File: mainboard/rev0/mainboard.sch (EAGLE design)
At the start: 11 parts

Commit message: cleaned up schematic
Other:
- note added: "Bluetooth"
- note added: "PWR Management"
- moved on the sheet: C1, C2, R1, R2, R3, R4, R5
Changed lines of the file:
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@@
 <sheet>
 <plain>
-<text x="-33.02" y="60.96" size="5.08" layer="97">MCU (MSP430F5528)</text>
+<text x="-121.92" y="58.42" size="5.08" layer="97">MCU (MSP430F5528)</text>
+<wire x1="-370.84" y1="48.26" x2="-370.84" y2="-63.5" width="0.1524" layer="97"/>
+<wire x1="-370.84" y1="-63.5" x2="-152.4" y2="-63.5" width="0.1524" layer="97"/>
+<wire x1="-152.4" y1="-63.5" x2="-152.4" y2="48.26" width="0.1524" layer="97"/>
+<wire x1="-152.4" y1="48.26" x2="-370.84" y2="48.26" width="0.1524" layer="97"/>
+<wire x1="-124.46" y1="55.88" x2="119.38" y2="55.88" width="0.1524" layer="97"/>
+<wire x1="119.38" y1="55.88" x2="119.38" y2="-68.58" width="0.1524" layer="97"/>
+<wire x1="119.38" y1="-68.58" x2="-124.46" y2="-68.58" width="0.1524" layer="97"/>
+<wire x1="-124.46" y1="-68.58" x2="-124.46" y2="55.88" width="0.1524" layer="97"/>
+<wire x1="-370.84" y1="-99.06" x2="-370.84" y2="-210.82" width="0.1524" layer="97"/>
+<wire x1="-370.84" y1="-210.82" x2="-152.4" y2="-210.82" width="0.1524" layer="97"/>
+<wire x1="-152.4" y1="-210.82" x2="-152.4" y2="-99.06" width="0.1524" layer="97"/>
+<wire x1="-152.4" y1="-99.06" x2="-370.84" y2="-99.06" width="0.1524" layer="97"/>
+<text x="-370.84" y="50.8" size="5.08" layer="97">PWR Management </text>
+<text x="-368.3" y="-93.98" size="5.08" layer="97">Bluetooth</text>
 </plain>
 <instances>
 <instance part="U$1" gate="G$1" x="0" y="0"/>
-<instance part="U$2" gate="G$1" x="134.62" y="-20.32"/>
-<instance part="U$3" gate="G$1" x="-187.96" y="-20.32"/>
-<instance part="SUPPLY1" gate="GND" x="-210.82" y="-43.18"/>
+<instance part="U$2" gate="G$1" x="-281.94" y="-180.34"/>
+<instance part="U$3" gate="G$1" x="-256.54" y="-12.7"/>
+<instance part="SUPPLY1" gate="GND" x="-279.4" y="-35.56"/>
 <instance part="SUPPLY2" gate="GND" x="45.72" y="-55.88"/>
-<instance part="SUPPLY3" gate="GND" x="180.34" y="-20.32"/>
-<instance part="JP1" gate="G$1" x="-274.32" y="-2.54" rot="MR0"/>
-<instance part="SUPPLY4" gate="GND" x="-269.24" y="-17.78"/>
-<instance part="C1" gate="G$1" x="-256.54" y="-7.62"/>
-<instance part="R1" gate="G$1" x="-124.46" y="7.62" rot="R90"/>
-<instance part="R2" gate="G$1" x="-124.46" y="-7.62" rot="R90"/>
-<instance part="R3" gate="G$1" x="-220.98" y="-27.94" rot="R270"/>
-<instance part="R4" gate="G$1" x="-231.14" y="-27.94" rot="R270"/>
-<instance part="R5" gate="G$1" x="-152.4" y="-38.1" rot="R270"/>
-<instance part="C2" gate="G$1" x="-106.68" y="-2.54"/>
+<instance part="SUPPLY3" gate="GND" x="-236.22" y="-180.34"/>
+<instance part="JP1" gate="G$1" x="-342.9" y="5.08" rot="MR0"/>
+<instance part="SUPPLY4" gate="GND" x="-337.82" y="-10.16"/>
+<instance part="C1" gate="G$1" x="-325.12" y="0"/>
+<instance part="R1" gate="G$1" x="-193.04" y="15.24" rot="R90"/>
+<instance part="R2" gate="G$1" x="-193.04" y="0" rot="R90"/>
+<instance part="R3" gate="G$1" x="-289.56" y="-20.32" rot="R270"/>
+<instance part="R4" gate="G$1" x="-299.72" y="-20.32" rot="R270"/>
+<instance part="R5" gate="G$1" x="-220.98" y="-30.48" rot="R270"/>
+<instance part="C2" gate="G$1" x="-175.26" y="5.08"/>
 </instances>
 <busses>
@@
 <segment>
 <pinref part="SUPPLY1" gate="GND" pin="GND"/>
-<wire x1="-210.82" y1="-40.64" x2="-210.82" y2="-38.1" width="0.1524" layer="91"/>
+<wire x1="-279.4" y1="-33.02" x2="-279.4" y2="-30.48" width="0.1524" layer="91"/>
 <pinref part="U$3" gate="G$1" pin="VSS@0"/>
-<wire x1="-210.82" y1="-38.1" x2="-210.82" y2="-35.56" width="0.1524" layer="91"/>
-<wire x1="-210.82" y1="-35.56" x2="-210.82" y2="-33.02" width="0.1524" layer="91"/>
-<wire x1="-210.82" y1="-33.02" x2="-205.74" y2="-33.02" width="0.1524" layer="91"/>
+<wire x1="-279.4" y1="-30.48" x2="-279.4" y2="-27.94" width="0.1524" layer="91"/>
+<wire x1="-279.4" y1="-27.94" x2="-279.4" y2="-25.4" width="0.1524" layer="91"/>
+<wire x1="-279.4" y1="-25.4" x2="-274.32" y2="-25.4" width="0.1524" layer="91"/>
 <pinref part="U$3" gate="G$1" pin="VSS@1"/>
-<wire x1="-205.74" y1="-35.56" x2="-210.82" y2="-35.56" width="0.1524" layer="91"/>
+<wire x1="-274.32" y1="-27.94" x2="-279.4" y2="-27.94" width="0.1524" layer="91"/>
 <pinref part="U$3" gate="G$1" pin="VSS@2"/>
-<wire x1="-210.82" y1="-38.1" x2="-205.74" y2="-38.1" width="0.1524" layer="91"/>
+<wire x1="-279.4" y1="-30.48" x2="-274.32" y2="-30.48" width="0.1524" layer="91"/>
 </segment>
 <segment>
@@
 <pinref part="U$2" gate="G$1" pin="GND@3"/>
 <pinref part="SUPPLY3" gate="GND" pin="GND"/>
-<wire x1="177.8" y1="-15.24" x2="180.34" y2="-15.24" width="0.1524" layer="91"/>
-<wire x1="180.34" y1="-15.24" x2="180.34" y2="-17.78" width="0.1524" layer="91"/>
+<wire x1="-238.76" y1="-175.26" x2="-236.22" y2="-175.26" width="0.1524" layer="91"/>
+<wire x1="-236.22" y1="-175.26" x2="-236.22" y2="-177.8" width="0.1524" layer="91"/>
 <pinref part="U$2" gate="G$1" pin="GND@2"/>
-<wire x1="177.8" y1="-12.7" x2="180.34" y2="-12.7" width="0.1524" layer="91"/>
-<wire x1="180.34" y1="-12.7" x2="180.34" y2="-15.24" width="0.1524" layer="91"/>
+<wire x1="-238.76" y1="-172.72" x2="-236.22" y2="-172.72" width="0.1524" layer="91"/>
+<wire x1="-236.22" y1="-172.72" x2="-236.22" y2="-175.26" width="0.1524" layer="91"/>
 <pinref part="U$2" gate="G$1" pin="GND@1"/>
-<wire x1="177.8" y1="-10.16" x2="180.34" y2="-10.16" width="0.1524" layer="91"/>
-<wire x1="180.34" y1="-10.16" x2="180.34" y2="-12.7" width="0.1524" layer="91"/>
+<wire x1="-238.76" y1="-170.18" x2="-236.22" y2="-170.18" width="0.1524" layer="91"/>
+<wire x1="-236.22" y1="-170.18" x2="-236.22" y2="-172.72" width="0.1524" layer="91"/>
 <pinref part="U$2" gate="G$1" pin="GND@0"/>
-<wire x1="177.8" y1="-7.62" x2="180.34" y2="-7.62" width="0.1524" layer="91"/>
-<wire x1="180.34" y1="-7.62" x2="180.34" y2="-10.16" width="0.1524" layer="91"/>
+<wire x1="-238.76" y1="-167.64" x2="-236.22" y2="-167.64" width="0.1524" layer="91"/>
+<wire x1="-236.22" y1="-167.64" x2="-236.22" y2="-170.18" width="0.1524" layer="91"/>
 </segment>
 <segment>
 <pinref part="JP1" gate="G$1" pin="GND"/>
-<wire x1="-271.78" y1="-2.54" x2="-269.24" y2="-2.54" width="0.1524" layer="91"/>
+<wire x1="-340.36" y1="5.08" x2="-337.82" y2="5.08" width="0.1524" layer="91"/>
 <pinref part="SUPPLY4" gate="GND" pin="GND"/>
-<wire x1="-269.24" y1="-2.54" x2="-269.24" y2="-12.7" width="0.1524" layer="91"/>
+<wire x1="-337.82" y1="5.08" x2="-337.82" y2="-5.08" width="0.1524" layer="91"/>
 <pinref part="C1" gate="G$1" pin="2"/>
-<wire x1="-269.24" y1="-12.7" x2="-269.24" y2="-15.24" width="0.1524" layer="91"/>
-<wire x1="-256.54" y1="-10.16" x2="-256.54" y2="-12.7" width="0.1524" layer="91"/>
-<wire x1="-256.54" y1="-12.7" x2="-269.24" y2="-12.7" width="0.1524" layer="91"/>
+<wire x1="-337.82" y1="-5.08" x2="-337.82" y2="-7.62" width="0.1524" layer="91"/>
+<wire x1="-325.12" y1="-2.54" x2="-325.12" y2="-5.08" width="0.1524" layer="91"/>
+<wire x1="-325.12" y1="-5.08" x2="-337.82" y2="-5.08" width="0.1524" layer="91"/>
 </segment>
 </net>
@@
 <segment>
 <pinref part="JP1" gate="G$1" pin="VBUS"/>
-<wire x1="-271.78" y1="0" x2="-256.54" y2="0" width="0.1524" layer="91"/>
+<wire x1="-340.36" y1="7.62" x2="-325.12" y2="7.62" width="0.1524" layer="91"/>
 <pinref part="C1" gate="G$1" pin="1"/>
-<wire x1="-256.54" y1="0" x2="-256.54" y2="-2.54" width="0.1524" layer="91"/>
+<wire x1="-325.12" y1="7.62" x2="-325.12" y2="5.08" width="0.1524" layer="91"/>
 </segment>
 </net>

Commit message: added the buttons garrett wanted
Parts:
- added C10, C11, C12, C13, C3, C4, C5, C6, C7, C8, C9: (no value), SparkFun-Capacitors:CAP0402-CAP
- added D1, D2: BLUE, SparkFun-LED:LED-BLUE0603
- added D4: (no value), SparkFun-DiscreteSemi:DIODEHV
- added L1: (no value), SparkFun-Passives:INDUCTOR-B82462G
- added R10, R6, R7, R8, R9: (no value), SparkFun-Passives:RESISTOR0402-RES
- added U$4, U$5, U$6, U$7: EVP-AEDB2A, TuansLib:EVP-AEDB2A
- added U$8: FH12-40S-0.5SH, TuansLib:FH12-40S-0.5SH
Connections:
- new net BATT_PWR: R6.2, U$3.BAT_IN, U$3.BAT_OUT
- new net BT_BAUD: U$1.P4.7/PM_NONE, U$2.PIO7
- new net BT_CONN: U$1.P4.6/PM_NONE, U$2.PIO2
- new net N$10: R4.1, U$3.STAT1
- new net N$11: R3.1, U$3.STAT2
- new net N$12: R6.1, U$3.EN
- new net N$13: R7.2, U$4.A
- new net N$14: R8.2, U$5.A
- new net N$15: R9.2, U$6.A
- new net N$16: R10.2, U$7.A
- new net N$17: R7.1
- new net N$18: R8.1
- new net N$19: R9.1
- new net N$2: D1.C, R4.2
- new net N$20: R10.1
- new net N$21: U$8.SCLK
- new net N$22: U$8.SI
- new net N$23: U$8.SO
- new net N$24: U$8.RESET
- new net N$25: U$8.ADC_IN
- new net N$26: C4.2, U$8.C42P
- new net N$27: C4.1, U$8.C42M
- new net N$28: C5.2, U$8.C41P
- new net N$29: C5.1, U$8.C41M
- new net N$3: D4.C, U$3.ISET2
- new net N$30: C6.2, U$8.C31M
- new net N$31: C6.1, U$8.C31P
- new net N$32: C7.2, U$8.C21M
- new net N$33: C7.1, U$8.C21P
- new net N$34: C8.2, U$8.C16M
- new net N$35: C8.1, U$8.C16P
- new net N$36: C9.1, U$8.C15M
- new net N$37: C9.2, U$8.C15P
- new net N$38: C10.1, U$8.C14M
- new net N$39: C10.2, U$8.C14P
- new net N$4: D2.C, R3.2
- new net N$40: C11.1, U$8.C13M
- new net N$41: C11.2, U$8.C13P
- new net N$42: C12.1, U$8.C12M
- new net N$43: C12.2, U$8.C12P
- new net N$44: C13.1, U$8.C11M
- new net N$45: C13.2, U$8.C11P
- new net N$46: C3.2, U$8.VCL
- new net N$5: R1.1, R2.2, U$3.FB
- new net N$6: L1.1, U$3.SW
- new net N$7: U$8.CSB
- new net N$8: U$8.BUSY
- new net SPI_CLK: U$1.P4.3/PM_UCB1CLK/PM_UCA1STE
- new net SPI_MISO: U$1.P4.2/PM_UCB1SOMI/PM_UCB1SCL
- new net SPI_MOSI: U$1.P4.1/PM_UCB1SIMO/PM_UCB1SDA
- new net SPI_STE: U$1.P4.0/PM_UCB1STE/PM_UCA1CLK
- new net UART_RX: U$1.P4.5/PM_UCA1RXD/PM_UCA1SOMI, U$2.UART_TX
- new net UART_TX: U$1.P4.4/PM_UCA1TXD/PM_UCA1SIMO, U$2.UART_RX
- new net VCC: C2.1, L1.2, R1.2, U$2.VCC@0
- new net VUSB: C1.1, D1.A, D2.A, D4.A, JP1.VBUS, U$3.USB
- net GND: now also C2.2, C3.1, R2.1, R5.2, U$3.CE, U$3.FPWM, U$4.B, U$5.B, U$6.B, U$7.B, U$8.ID
- net N$1: now also R5.1, U$3.ISET1; no longer C1.1, JP1.VBUS
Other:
- note added: "Buttons"
- note added: "Display"
- note added: "PWR Monitoring"
- note added: "Sensor"
- moved on the sheet: C1, C2, R1, R2, R3, R4, R5

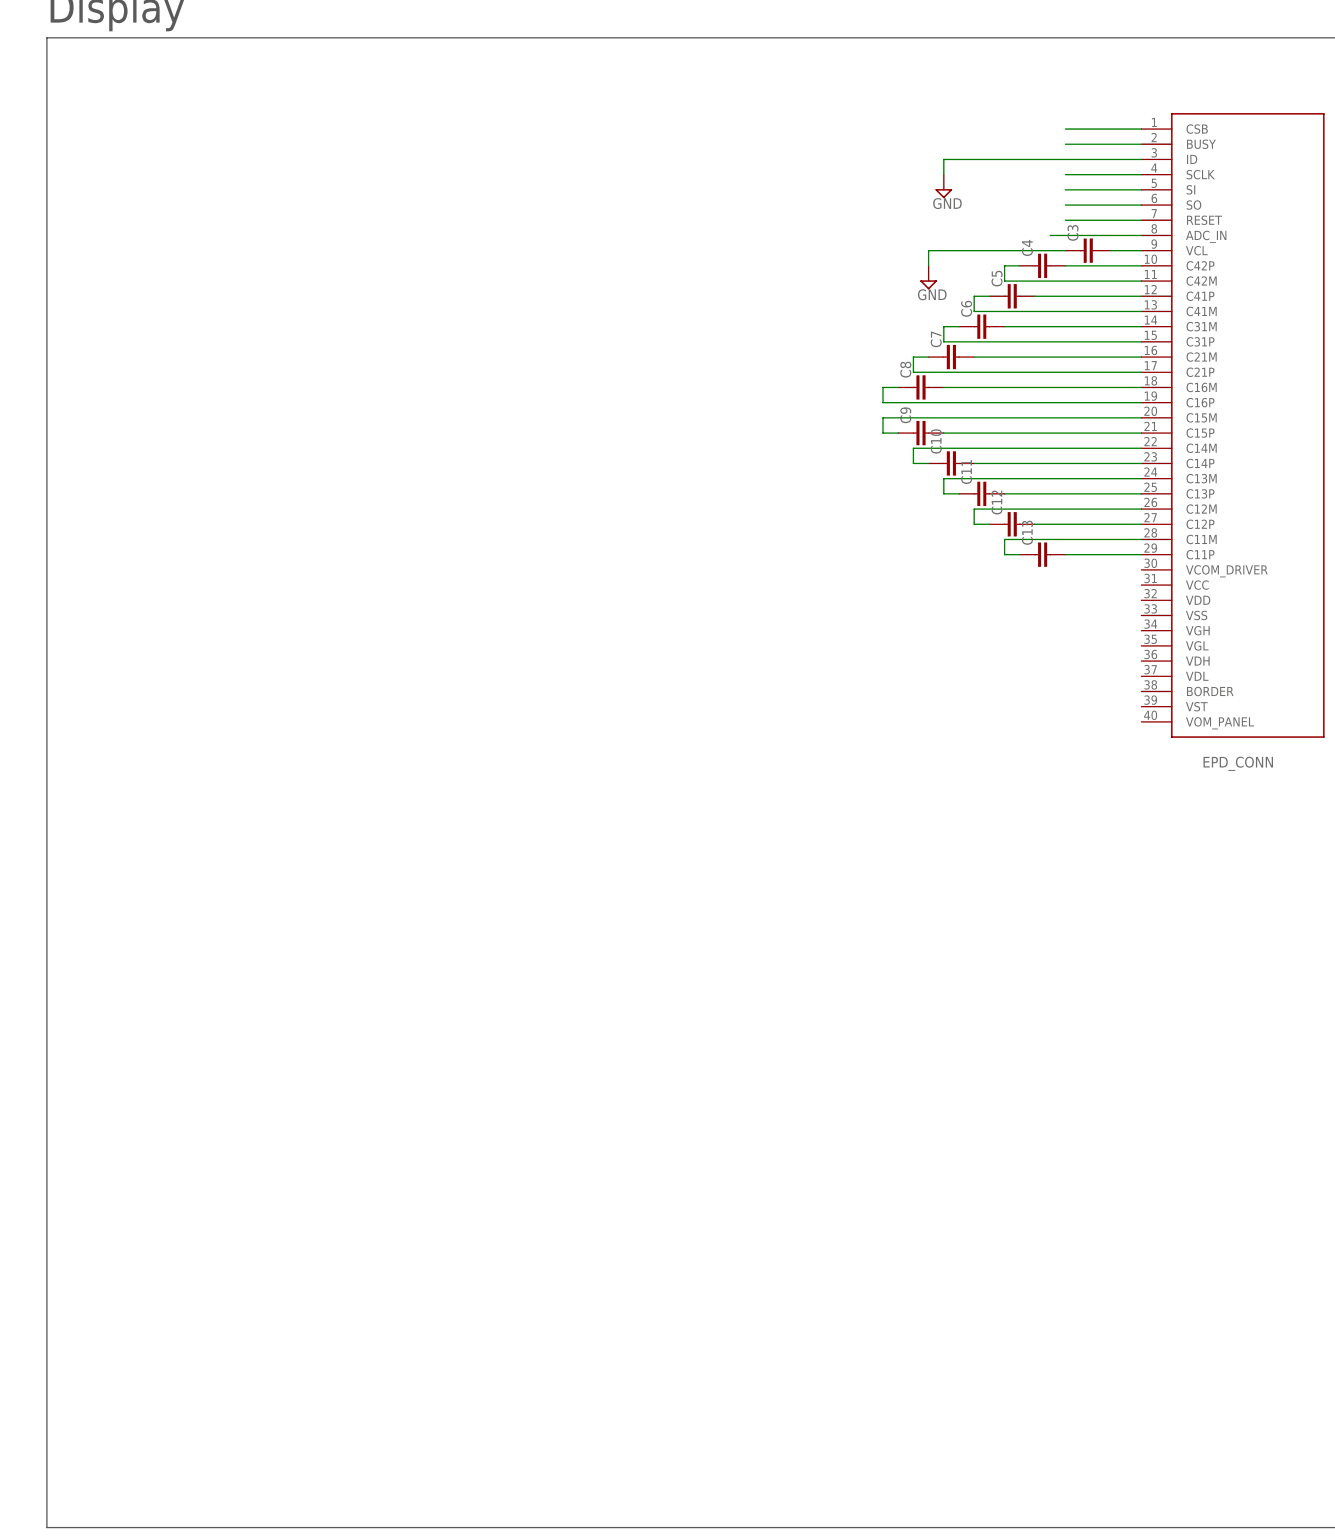
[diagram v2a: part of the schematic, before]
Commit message: Completed EPD connector schematic needs to be reviewed before sent out
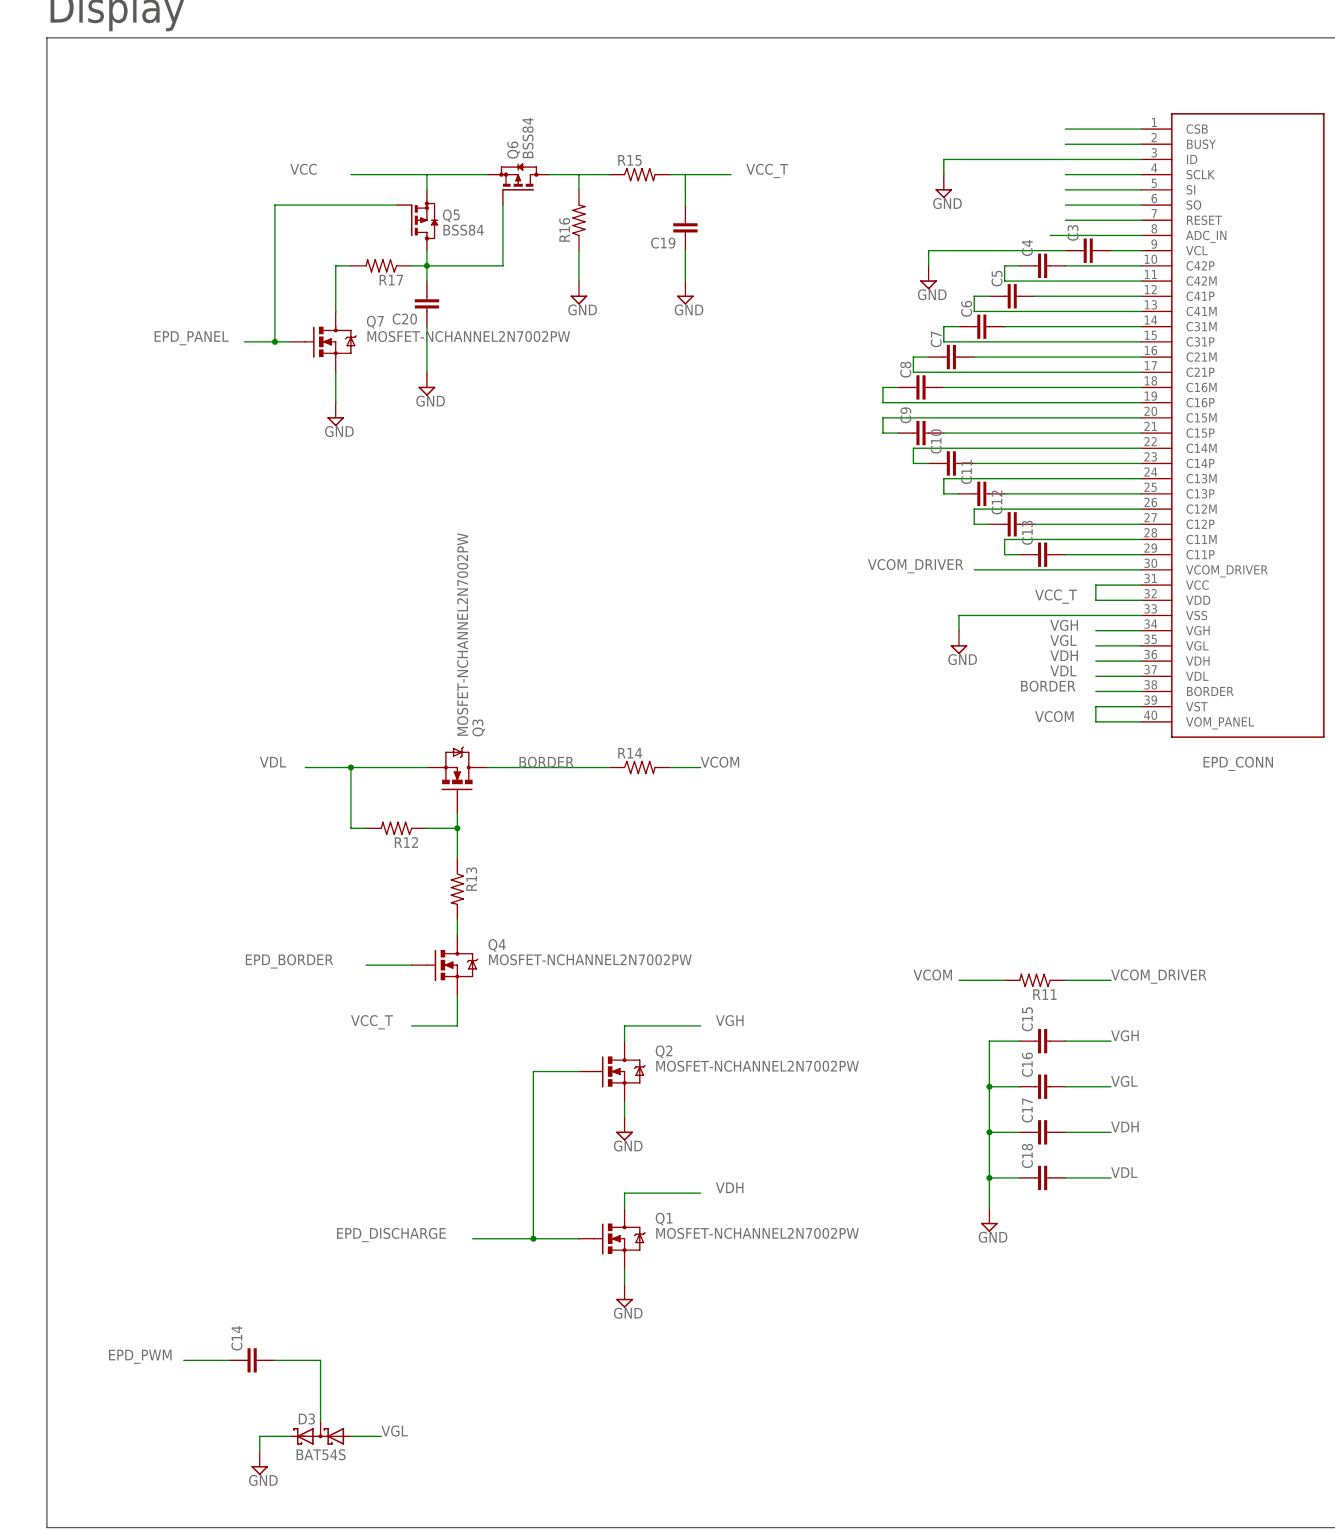
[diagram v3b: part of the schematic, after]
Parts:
- added C14, C15, C16, C17, C18, C19, C20: (no value), SparkFun-Capacitors:CAP0402-CAP
- added D3: BAT54S, diode:BAT54S
- added Q1, Q2, Q3, Q4, Q7: MOSFET-NCHANNEL2N7002PW, SparkFun-DiscreteSemi:MOSFET-NCHANNEL2N7002PW
- added Q5, Q6: BSS84, transistor-small-signal:BSS84
- added R11, R12, R13, R14, R15, R16, R17: (no value), SparkFun-Passives:RESISTOR0402-RES
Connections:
- new net BORDER: Q3.D, R14.1, U$8.BORDER
- new net EPD_BORDER: Q4.G
- new net EPD_DISCHARGE: Q1.G, Q2.G
- new net EPD_PANEL: Q5.G, Q7.G
- new net EPD_PWM: C14.1
- new net N$47: Q6.D, R15.1, R16.2
- new net N$49: Q3.G, R12.1, R13.1
- new net N$50: C20.2, Q5.D, Q6.G, R17.1
- new net N$52: Q7.D, R17.2
- new net N$53: Q4.D, R13.2
- new net N$9: C14.2, D3.C1A2
- new net VCC_T: C19.2, Q4.S, R15.2, U$8.VCC, U$8.VDD
- new net VCOM: R11.2, R14.2, U$8.VOM_PANEL, U$8.VST
- new net VCOM_DRIVER: U$8.VCOM_DRIVER
- new net VDH: C17.2, Q1.D, U$8.VDH
- new net VDL: C18.2, Q3.S, R12.2, U$8.VDL
- new net VGH: C15.2, Q2.D, U$8.VGH
- new net VGL: C16.2, D3.A1, U$8.VGL
- net GND: now also C15.1, C16.1, C17.1, C18.1, C19.1, C20.1, D3.C2, Q1.S, Q2.S, Q7.S, R16.1, U$8.VSS
- net VCC: now also Q5.S, Q6.S

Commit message: rarrrrrarararaaawww.
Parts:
- removed Q6: BSS84, transistor-small-signal:BSS84
- added C21, C22, C23, C24, C25, C26, C27, C28, C29, C30: (no value), SparkFun-Capacitors:CAP0402-CAP
- added D5, D6, D7, D8: BLUE, SparkFun-LED:LED-BLUE0603
- added JP2: M02PTH, SparkFun-Connectors:M02PTH
- added JP3: (no value), SparkFun-Connectors:M03PTH
- added R18, R19, R20, R21, R22, R23, R24, R25, R26, R27: (no value), SparkFun-Passives:RESISTOR0402-RES
- added U$10: DMG2305UX, TuansLib:DMG2305UX
- added U$9: BQ27410, TuansLib:BQ27410
- Q4: value MOSFET-NCHANNEL2N7002PW -> BSS84; device SparkFun-DiscreteSemi:MOSFET-NCHANNEL2N7002PW -> transistor-small-signal:BSS84
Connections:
- removed net N$17: R7.1
- removed net N$18: R8.1
- removed net N$19: R9.1
- removed net N$20: R10.1
- removed net N$21: U$8.SCLK
- removed net N$22: U$8.SI
- removed net N$23: U$8.SO
- removed net N$24: U$8.RESET
- removed net N$8: U$8.BUSY
- removed net SPI_STE: U$1.P4.0/PM_UCB1STE/PM_UCA1CLK
- new net BTN_0: R7.1, U$1.P2.0/TA1.1
- new net BTN_1: R8.1, U$1.P2.1/TA1.2
- new net BTN_2: R9.1, U$1.P2.2/TAC2CLK/SMCLK
- new net BTN_3: R10.1, U$1.P2.3/TA2.0
- new net EPD_BUSY: U$1.P6.4/CB4/A4, U$8.BUSY
- new net EPD_CS: U$1.P6.2/CB2/A2, U$8.CSB
- new net EPD_RST: U$1.P6.5/CB5/A5, U$8.RESET
- new net LED_0: D5.C, U$1.P2.4/TA2.1
- new net LED_1: D6.C, U$1.P2.5/TA2.2
- new net LED_2: D7.C, U$1.P2.6/RTCOLK/DMAE0
- new net LED_3: D8.C, U$1.P2.7/UCB0STE/UCA0CLK
- new net N$48: D5.A, R23.1
- new net N$51: D6.A, R24.1
- new net N$54: C23.1, R18.1, U$9.SRP
- new net N$55: D7.A, R25.1
- new net N$56: D8.A, R26.1
- new net PM_BIN: R21.2, U$1.P3.3/UCA0TXD/UCA0SIMO, U$9.BIN
- new net PM_GPOUT: R22.2, U$1.P3.2/UCB0CLK/UCA0STE, U$9.GPOUT
- new net PM_SCL: R19.2, U$1.P3.1/UCB0SOMI/UCB0SCL, U$9.SCL
- new net PM_SDA: R20.2, U$1.P3.0/UCB0SIMO/UCB0SDA, U$9.SDA
- new net SENSOR_DATA: JP3.2, U$1.P6.0/CB0/A0, U$1.P6.1/CB1/A1
- new net VCC_R: C25.1, U$9.REG25, U$9.VCC
- net BATT_PWR: now also C22.1, C24.1, JP2.2, U$9.BAT, U$9.REGIN
- net BORDER: now also R27.1
- net EPD_BORDER: now also U$1.P6.6/CB6/A6
- net EPD_DISCHARGE: now also U$1.P6.7/CB7/A7
- net EPD_PANEL: now also U$1.P6.3/CB3/A3
- net EPD_PWM: now also U$1.P1.1/TA0.0
- net GND: now also C21.2, C22.2, C23.2, C24.2, C25.2, C26.2, C27.2, C28.2, C29.2, C30.1, JP2.1, JP3.1, R18.2, U$9.NC, U$9.PWR_PAD, U$9.SRN, U$9.VSS
- net N$25: now also R27.2
- net N$47: now also U$10.SOURCE; no longer Q6.D
- net N$50: now also U$10.GATE; no longer Q6.G
- net N$53: now also Q4.S; no longer Q4.D
- net N$7: now also C30.2, U$1.VCORE; no longer U$8.CSB
- net SPI_CLK: now also U$8.SCLK
- net SPI_MISO: now also U$8.SO
- net SPI_MOSI: now also U$8.SI
- net VCC: now also C26.1, C27.1, C28.1, C29.1, JP3.3, R19.1, R20.1, R21.1, R22.1, R23.2, R24.2, R25.2, R26.2, U$1.AVCC1, U$1.DVCC1, U$1.DVCC2, U$10.DRAIN; no longer Q6.S
- net VCC_T: now also Q4.D; no longer Q4.S
- net VCOM: now also C21.1
- net VCOM_DRIVER: now also R11.1
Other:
- note added: "Buttons & LED"
- note added: "add AP2305"
- note removed: "Buttons"
- moved on the sheet: C20, Q5, Q7, R10, R17, R7, R8, R9
